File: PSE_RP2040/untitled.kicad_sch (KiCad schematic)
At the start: 21 parts, among them U7 TPS2375-1, U8 LMR16006YQ

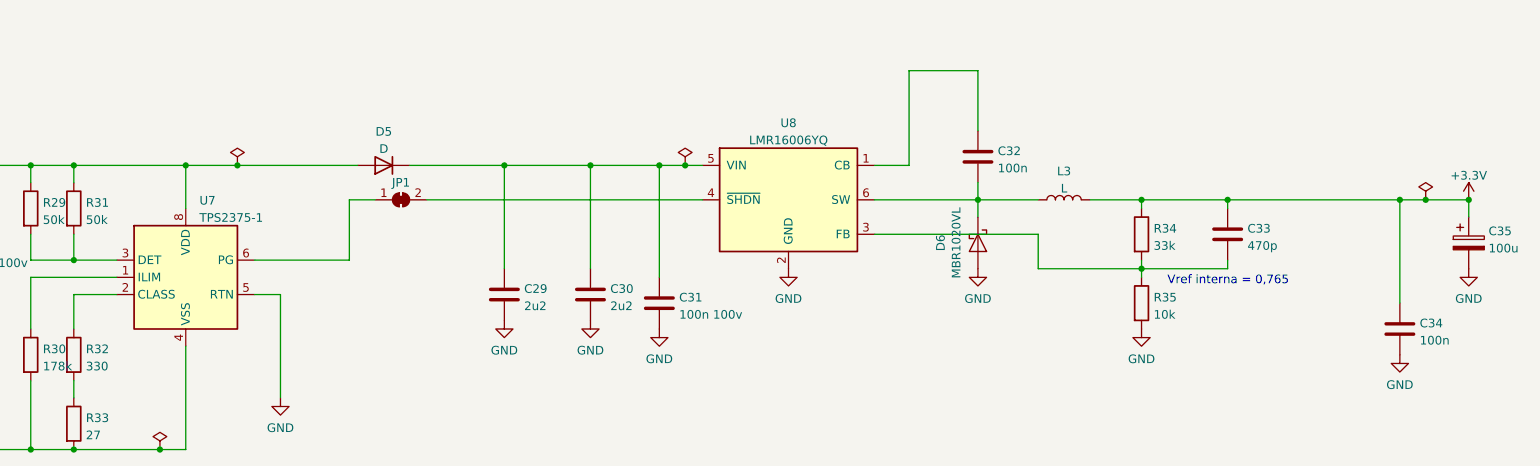
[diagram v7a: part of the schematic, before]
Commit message: annotato schematico + pwr flag
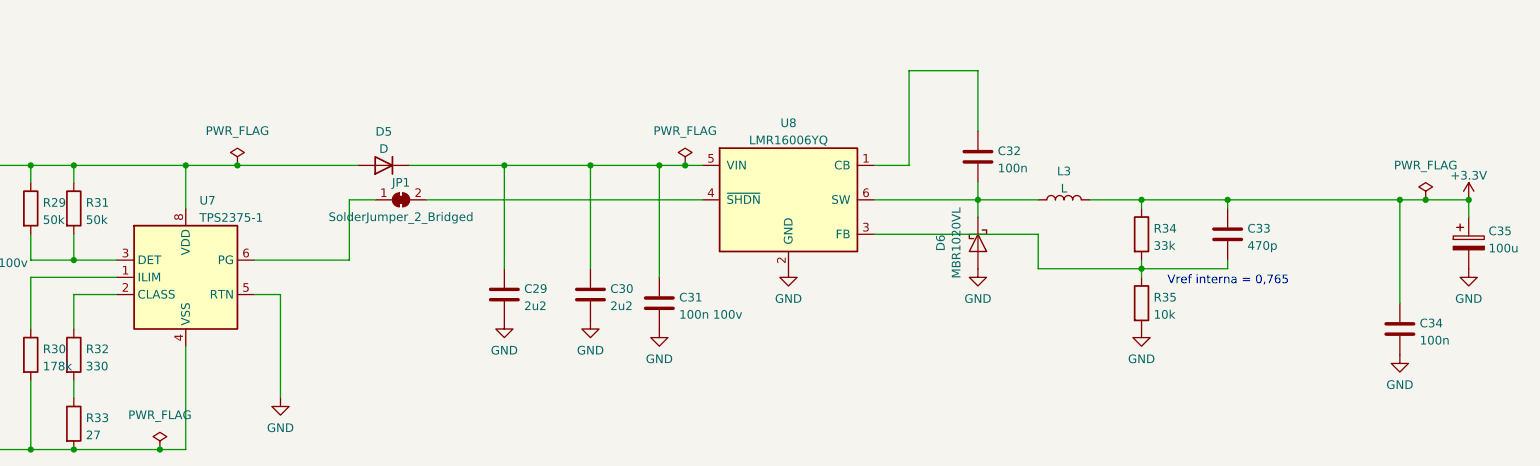
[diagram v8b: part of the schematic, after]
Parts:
- JP1: value (none) -> SolderJumper_2_Bridged
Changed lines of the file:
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@@
     (in_bom yes) (on_board yes)
     (property "Reference" "JP1" (id 0) (at 114.3 48.26 0))
-    (property "Value" "" (id 1) (at 114.3 53.34 0))
+    (property "Value" "SolderJumper_2_Bridged" (id 1) (at 114.3 53.34 0))
     (property "Footprint" "" (id 2) (at 114.3 50.8 0)
       (effects (font (size 1.27 1.27)) hide)
@@
       (effects (font (size 1.27 1.27)) hide)
     )
-    (property "Value" "" (id 1) (at 78.74 82.55 0))
+    (property "Value" "PWR_FLAG" (id 1) (at 78.74 82.55 0))
     (property "Footprint" "" (id 2) (at 78.74 87.63 0)
       (effects (font (size 1.27 1.27)) hide)
@@
       (effects (font (size 1.27 1.27)) hide)
     )
-    (property "Value" "" (id 1) (at 156.21 40.64 0))
+    (property "Value" "PWR_FLAG" (id 1) (at 156.21 40.64 0))
     (property "Footprint" "" (id 2) (at 156.21 45.72 0)
       (effects (font (size 1.27 1.27)) hide)
@@
       (effects (font (size 1.27 1.27)) hide)
     )
-    (property "Value" "" (id 1) (at 90.17 40.64 0))
+    (property "Value" "PWR_FLAG" (id 1) (at 90.17 40.64 0))
     (property "Footprint" "" (id 2) (at 90.17 45.72 0)
       (effects (font (size 1.27 1.27)) hide)
@@
       (effects (font (size 1.27 1.27)) hide)
     )
-    (property "Value" "" (id 1) (at 265.43 45.72 0))
+    (property "Value" "PWR_FLAG" (id 1) (at 265.43 45.72 0))
     (property "Footprint" "" (id 2) (at 265.43 50.8 0)
       (effects (font (size 1.27 1.27)) hide)
